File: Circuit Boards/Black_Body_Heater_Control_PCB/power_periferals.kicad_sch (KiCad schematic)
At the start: 29 parts, among them J301 Conn_01x02_Pin, P301 436500200, P302 436500200, Q302 BD139, U301 DAC60501ZDGSR, U302 INA181A2IDBVR, U305 LM358

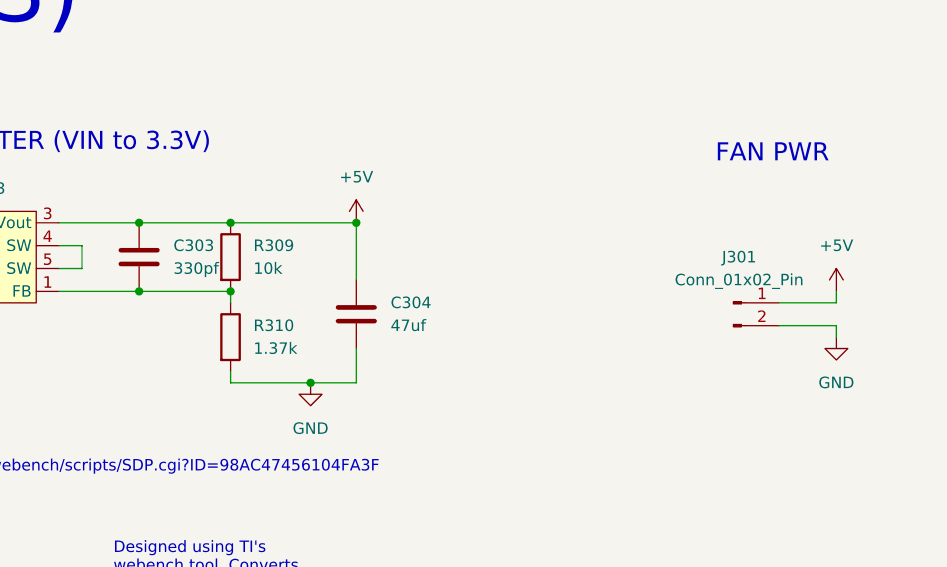
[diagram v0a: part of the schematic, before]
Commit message: Heater control rev 1 ordered
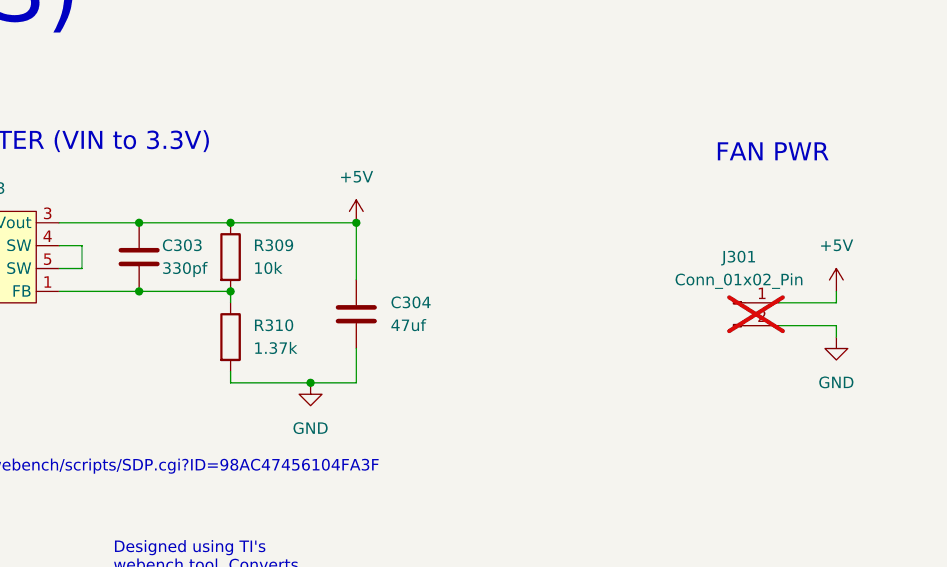
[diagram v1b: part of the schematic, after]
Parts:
- C302: MPN (none) -> C1608X5R1E685K080AC
- C303: MPN (none) -> C0603C331J5GACTU
- C304: MPN (none) -> GRM32EC81C476KE15L
- J301: now not fitted; now left out of the parts list
- R309: MPN (none) -> ERA-3AEB103V
- R310: MPN (none) -> ERJ-3EKF1371V
- U303: MPN (none) -> TPSM84209RKHR
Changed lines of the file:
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@@
+			)
+		)
+		(property "MPN" "ERA-3AEB103V"
+			(at 182.88 55.88 0)
+			(hide yes)
+			(show_name no)
+			(do_not_autoplace no)
+			(effects
+				(font
+					(size 1.27 1.27)
+				)
 			)
 		)
@@
 			)
 		)
+		(property "MPN" "ERJ-3EKF1371V"
+			(at 182.88 64.77 0)
+			(hide yes)
+			(show_name no)
+			(do_not_autoplace no)
+			(effects
+				(font
+					(size 1.27 1.27)
+				)
+			)
+		)
 		(pin "1"
 		)
@@
 		(body_style 1)
 		(exclude_from_sim no)
-		(in_bom yes)
-		(on_board yes)
-		(in_pos_files yes)
-		(dnp no)
+		(in_bom no)
+		(on_board yes)
+		(in_pos_files yes)
+		(dnp yes)
 		(fields_autoplaced yes)
 		(property "Reference" "J301"
@@
 			)
 		)
+		(property "MPN" "C1608X5R1E685K080AC"
+			(at 135.89 55.88 0)
+			(hide yes)
+			(show_name no)
+			(do_not_autoplace no)
+			(effects
+				(font
+					(size 1.27 1.27)
+				)
+			)
+		)
 		(pin "2"
 		)
@@
 		(in_pos_files yes)
 		(dnp no)
-		(fields_autoplaced yes)
 		(property "Reference" "C303"
-			(at 176.53 54.6099 0)
+			(at 175.26 54.61 0)
 			(show_name no)
 			(do_not_autoplace no)
@@
 		)
 		(property "Value" "330pf"
-			(at 176.53 57.1499 0)
+			(at 175.26 57.15 0)
 			(show_name no)
 			(do_not_autoplace no)
@@
 		)
 		(property "Description" "Unpolarized capacitor"
+			(at 172.72 55.88 0)
+			(hide yes)
+			(show_name no)
+			(do_not_autoplace no)
+			(effects
+				(font
+					(size 1.27 1.27)
+				)
+			)
+		)
+		(property "MPN" "C0603C331J5GACTU"
 			(at 172.72 55.88 0)
 			(hide yes)
@@
 			)
 		)
+		(property "MPN" "TPSM84209RKHR"
+			(at 154.94 55.88 0)
+			(hide yes)
+			(show_name no)
+			(do_not_autoplace no)
+			(effects
+				(font
+					(size 1.27 1.27)
+				)
+			)
+		)
 		(pin "6"
 		)
@@
 			(at 196.85 62.23 0)
 			(hide yes)
+			(show_name no)
+			(do_not_autoplace no)
+			(effects
+				(font
+					(size 1.27 1.27)
+				)
+			)
+		)
+		(property "MPN" "GRM32EC81C476KE15L"
+			(at 196.85 62.23 0)
+			(hide yes)
